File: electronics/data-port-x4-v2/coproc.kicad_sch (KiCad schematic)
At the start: 47 parts, among them J2 SWD, U11 RP2354B, Y2 ABM8-272-T3

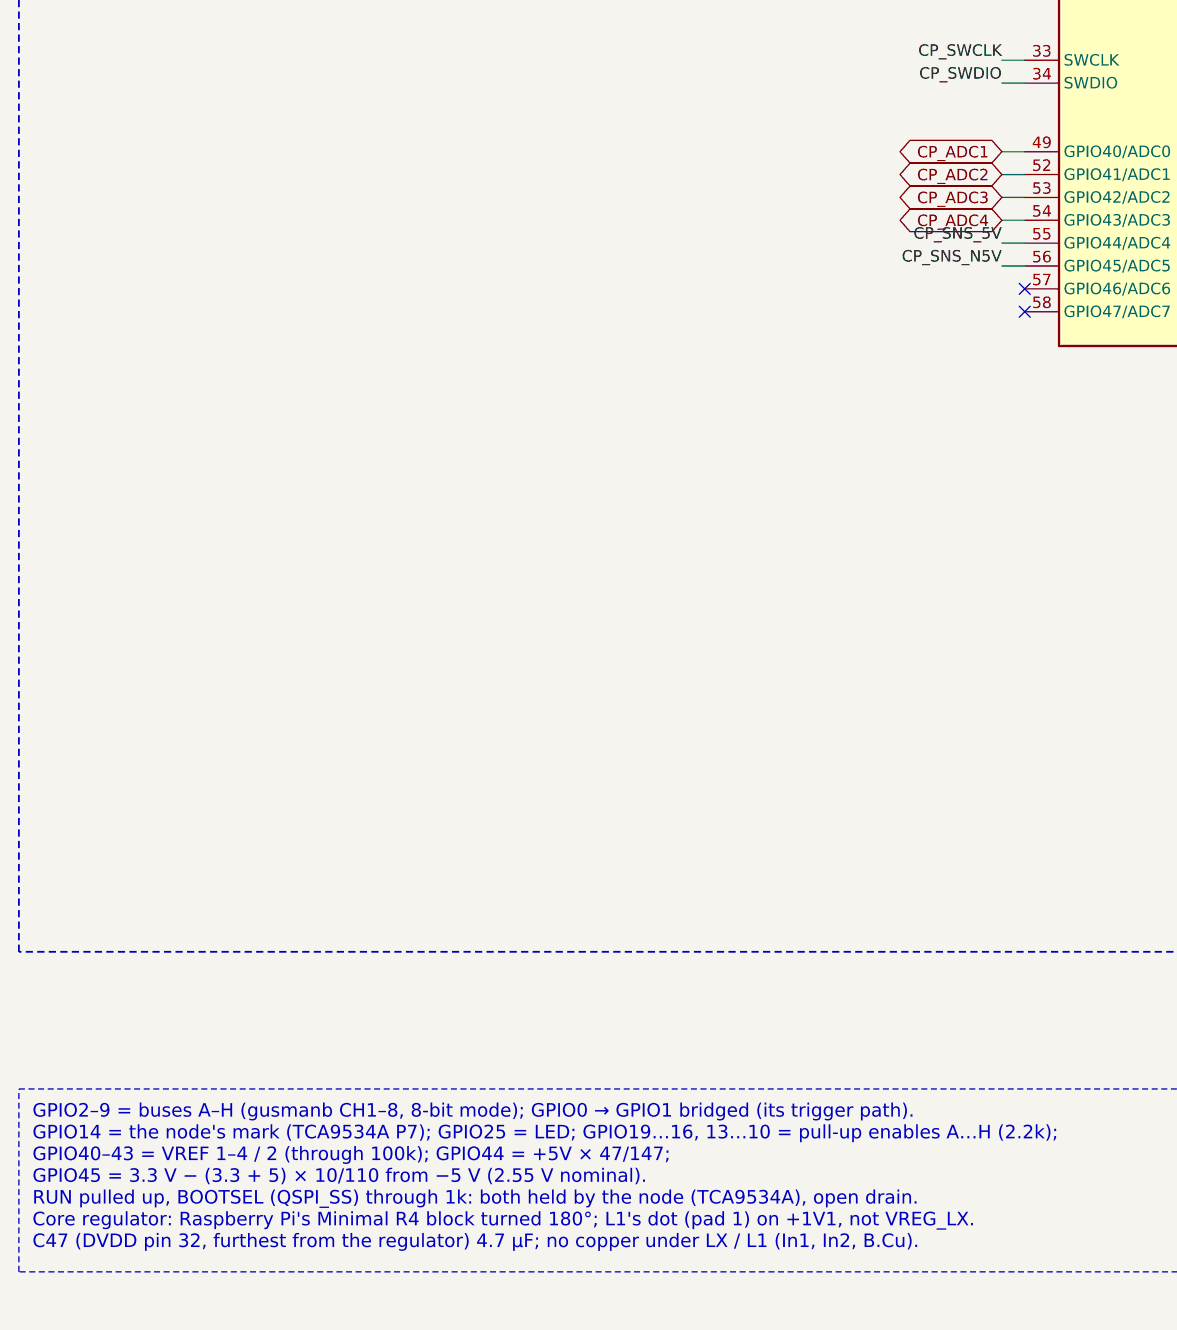
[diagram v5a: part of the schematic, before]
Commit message: DATA x4 v2: C45 at the co-processor's DVDD pin 51, VREF2 and VREF4 on swapped GPIOs
C45 (100 nF, +1V1) sat 4.83 mm south of U11's DVDD pin 51 (U11: the
RP2354B); its path to the pin ran 7.9 mm through two vias.  It now
stands right west of the pin, 0.51 mm, on the pin's own line, its GND
via below it.  To make room, the west face's lines below it are drawn:
VREF4 (pin 52) and VREF2 (pin 54) each drop to B.Cu right by their
pin, 4's via east and 2's west, and run on south as before; for those
two runs not to cross, their GPIOs swap (VREF2 now on GPIO43, VREF4 on
GPIO41: the user's go-ahead, 2026-10-28; no firmware maps them yet,
the co-processor spike leaves the VREF reads out).  BUS_C's dive to
B.Cu moves west of C45, and R39's GND via is drawn where its fan-out
had it (BUS_C's via now pushed the automatic one onto CP_SNS_5V).

Pin 51 keeps its via under the case into the +1V1 network: there is no
room for a via after C45 (C36's +3V3_CP line north, the VREF vias
south), so C45 stays the pin -> cap -> via rule's one exception.

ERC 0, DRC 0, unconnected 0, no antenna; panel DRC 0.  The board stays
pending in electronics/decoupling.json (4 left by distance: C40, C41,
C44, C46).

Co-Authored-By: Claude Opus 5.5 <noreply@anthropic.com>
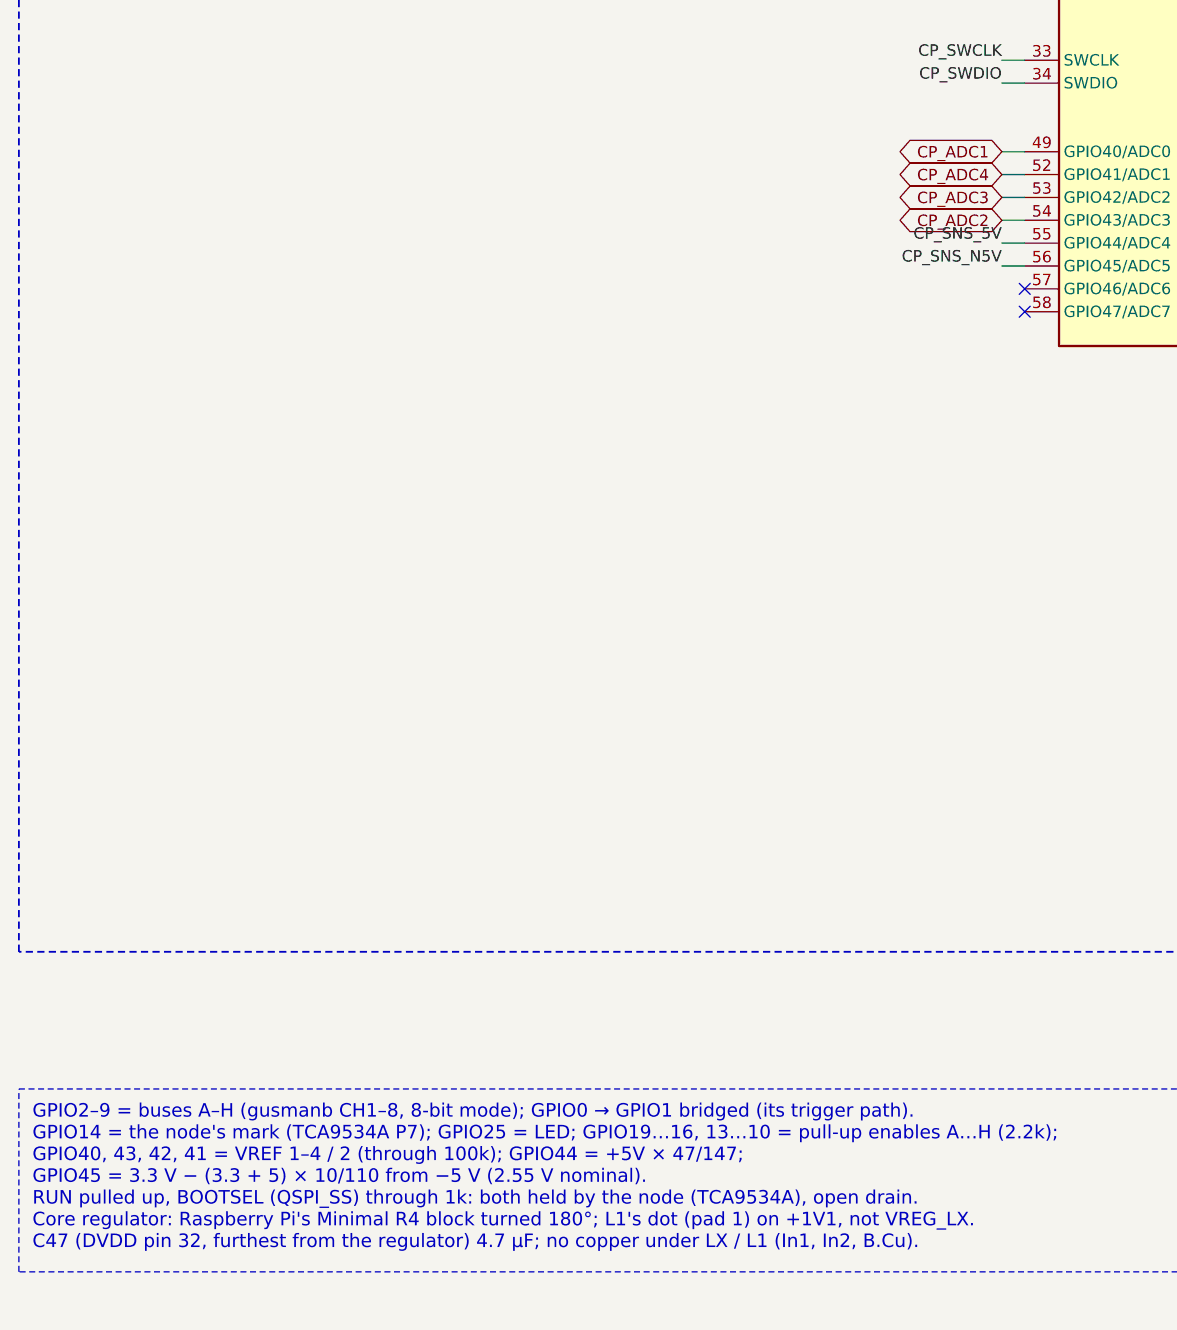
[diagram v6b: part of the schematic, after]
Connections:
- net CP_ADC2: now also U11.54 (GPIO43/ADC3); no longer U11.52 (GPIO41/ADC1)
- net CP_ADC4: now also U11.52 (GPIO41/ADC1); no longer U11.54 (GPIO43/ADC3)
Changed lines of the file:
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@@
 		)
 	)
-	(global_label "CP_ADC2"
+	(global_label "CP_ADC4"
 		(shape bidirectional)
 		(at 124.46 213.36 180)
@@
 		)
 	)
-	(global_label "CP_ADC4"
+	(global_label "CP_ADC2"
 		(shape bidirectional)
 		(at 124.46 218.44 180)
@@
 		)
 	)
-	(text_box "GPIO2–9 = buses A–H (gusmanb CH1–8, 8-bit mode); GPIO0 → GPIO1 bridged (its trigger path).\nGPIO14 = the node's mark (TCA9534A P7); GPIO25 = LED; GPIO19…16, 13…10 = pull-up enables A…H (2.2k);\nGPIO40–43 = VREF 1–4 / 2 (through 100k); GPIO44 = +5V × 47/147;\n  GPIO45 = 3.3 V − (3.3 + 5) × 10/110 from −5 V (2.55 V nominal).\nRUN pulled up, BOOTSEL (QSPI_SS) through 1k: both held by the node (TCA9534A), open drain.\nCore regulator: Raspberry Pi's Minimal R4 block turned 180°; L1's dot (pad 1) on +1V1, not VREG_LX.\nC47 (DVDD pin 32, furthest from the regulator) 4.7 µF; no copper under LX / L1 (In1, In2, B.Cu)."
+	(text_box "GPIO2–9 = buses A–H (gusmanb CH1–8, 8-bit mode); GPIO0 → GPIO1 bridged (its trigger path).\nGPIO14 = the node's mark (TCA9534A P7); GPIO25 = LED; GPIO19…16, 13…10 = pull-up enables A…H (2.2k);\nGPIO40, 43, 42, 41 = VREF 1–4 / 2 (through 100k); GPIO44 = +5V × 47/147;\n  GPIO45 = 3.3 V − (3.3 + 5) × 10/110 from −5 V (2.55 V nominal).\nRUN pulled up, BOOTSEL (QSPI_SS) through 1k: both held by the node (TCA9534A), open drain.\nCore regulator: Raspberry Pi's Minimal R4 block turned 180°; L1's dot (pad 1) on +1V1, not VREG_LX.\nC47 (DVDD pin 32, furthest from the regulator) 4.7 µF; no copper under LX / L1 (In1, In2, B.Cu)."
 		(exclude_from_sim no)
 		(at 15.24 314.96 0)
